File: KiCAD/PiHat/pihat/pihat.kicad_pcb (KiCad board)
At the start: 2 copper layers, 65 x 56 mm, 13 parts, among them P1 Conn_02x20_Odd_Even, Q1 BSS138, Q2 BSS138, U1 SG-92R, U2 SF3218MG

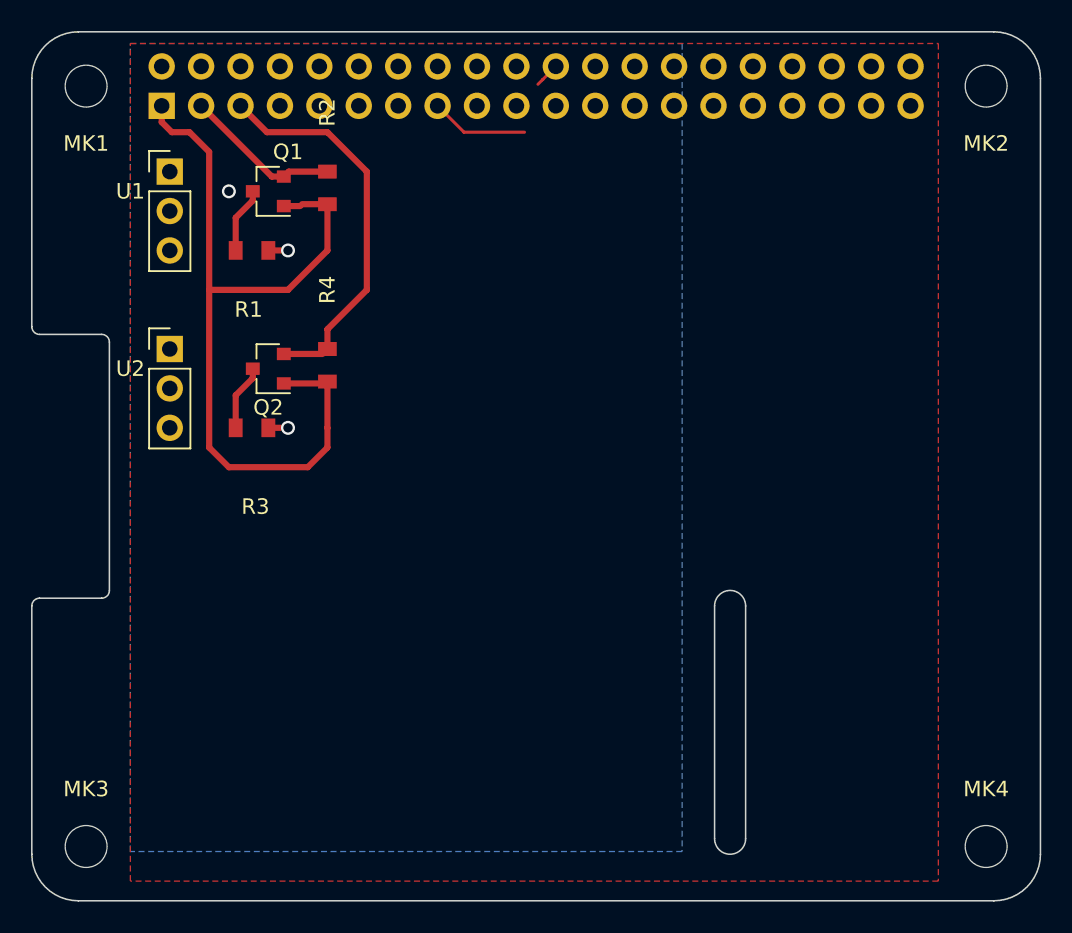
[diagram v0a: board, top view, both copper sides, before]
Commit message: compacted servo design
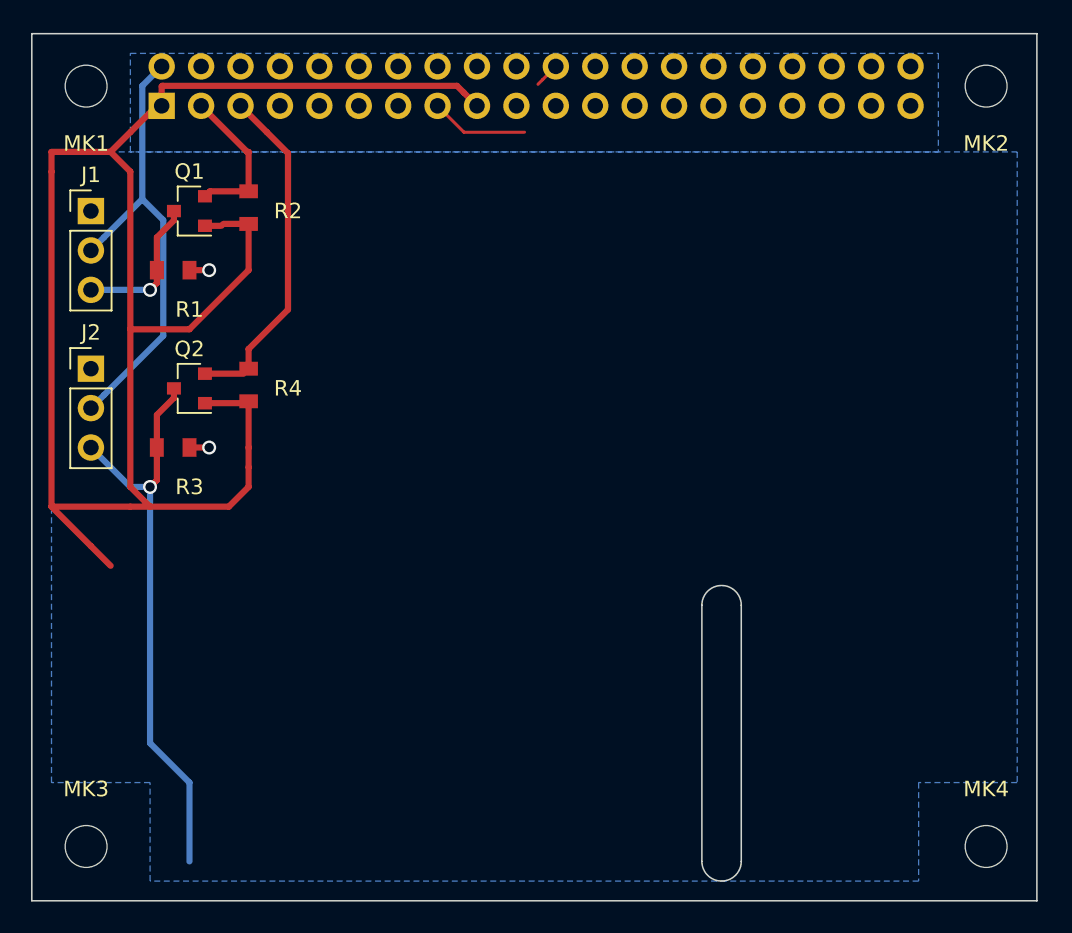
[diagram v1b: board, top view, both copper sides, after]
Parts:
- removed U1: SG-92R, trailTracer:PinHeader_1x03_P2.54mm_Vertical
- removed U2: SF3218MG, trailTracer:PinHeader_1x03_P2.54mm_Vertical
- added J1: Conn_01x03, Connector_PinHeader_2.54mm:PinHeader_1x03_P2.54mm_Vertical, F.Cu at (203.8, 105.5)
- added J2: Conn_01x03, Connector_PinHeader_2.54mm:PinHeader_1x03_P2.54mm_Vertical, F.Cu at (203.8, 115.7)
- moved Q2 5.24 mm to (210.2, 117.0)
- moved Q1 5.24 mm to (210.2, 105.5)
- moved R2 5.24 mm to (214.0, 104.3)
- moved R4 5.24 mm to (214.0, 115.7)
- moved R3 5.24 mm to (208.1, 120.8)
- moved R1 5.24 mm to (208.1, 109.4)
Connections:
- net /GPIO11(SPI0_SCK) renamed GPIO_11
- net /GPIO13(PWM1) renamed GPIO_13
- net /GPIO17(GEN0) renamed GPIO_17
- net /GPIO27(GEN2) renamed GPIO_27
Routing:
- net +3V3: track 54.2 -> 118.3 mm
- net Net-(J2-Pad3): track 4.27 -> 37.0 mm, vias 0 -> 1
- net +5V: track 2.54 -> 32.2 mm
- net Net-(J1-Pad3): track 4.27 -> 9.53 mm, vias 0 -> 1
- net GPIO_3: track 25.3 -> 22.2 mm
- net (no net): vias 1 -> 0
- added copper zone on B.Cu, net GND
- removed copper zone on B.Cu, net +5V
- removed copper zone on F.Cu, net GND
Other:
- board size 65 x 56 mm -> 64.8 x 55.9 mm
- board text removed: "DISPLAY"
- board text removed: "RJ45"
- board text removed: "USB"

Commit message: Added Fan Header
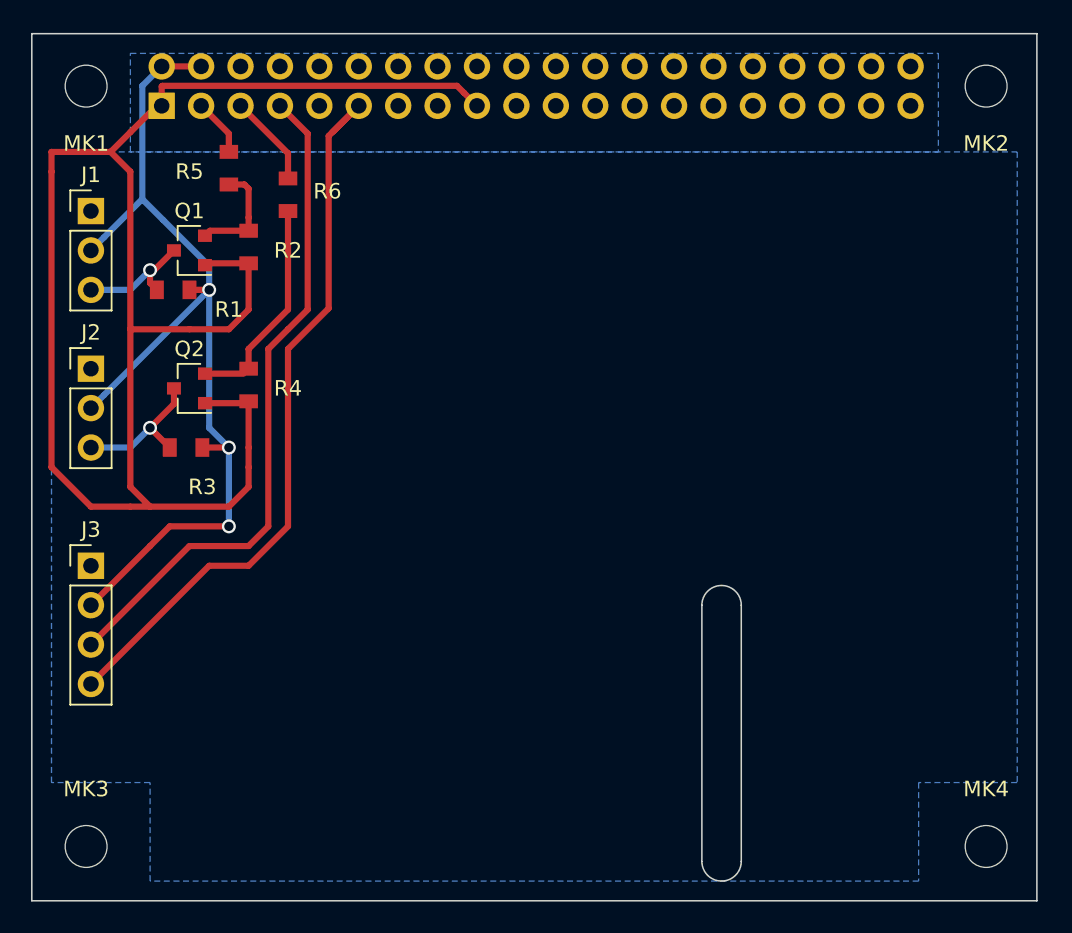
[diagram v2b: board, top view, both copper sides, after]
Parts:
- added J3: Fan, Connector_PinHeader_2.54mm:PinHeader_1x04_P2.54mm_Vertical, F.Cu at (203.8, 128.4)
- added R5: 220R, trailTracer:Yageo_R0805, F.Cu at (212.7, 103.8)
- added R6: 220R, trailTracer:Yageo_R0805, F.Cu at (216.5, 105.5)
- J1: value Conn_01x03 -> Pan Servo Connector
- J2: value Conn_01x03 -> Tilt Servo Connector
- moved Q1 2.54 mm to (210.2, 108.1)
- moved R2 2.54 mm to (214.0, 106.8)
- moved R1 1.27 mm to (208.1, 110.6)
- moved R3 0.83 mm to (208.9, 120.8)
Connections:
- P1 pad 7: /GPIO4(GCLK) -> GPIO_4
- Q1 pad 2: GPIO_2 -> Net-(Q1-Pad2)
- Q2 pad 2: GPIO_3 -> Net-(Q2-Pad2)
- R2 pad 1: GPIO_2 -> Net-(Q1-Pad2)
- R4 pad 1: GPIO_3 -> Net-(Q2-Pad2)
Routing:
- net GPIO_17: track 0.00 -> 48.3 mm
- net GPIO_4: track 0.00 -> 43.5 mm
- net +5V: track 32.2 -> 64.4 mm, vias 2 -> 3
- net Net-(J2-Pad3): track 37.0 -> 9.31 mm
- net GPIO_3: track 22.2 -> 5.95 mm
- net Net-(Q2-Pad2): track 0.00 -> 14.2 mm
- net +3V3: track 118.3 -> 110.4 mm
- net Net-(Q1-Pad2): track 0.00 -> 7.03 mm
- net GPIO_22: track 6.30 -> 0.00 mm
- net GPIO_2: track 9.77 -> 3.71 mm
- net Net-(J1-Pad3): track 9.53 -> 7.85 mm
- net GPIO_25: track 1.63 -> 0.00 mm

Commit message: Temporary Commit
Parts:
- added J4: Power Connector, Connector_JST:JST_VH_S2P-VH_1x02_P3.96mm_Horizontal, F.Cu at (249.5, 136.0)
- added U1: TPS5431DDA, Package_SO:TI_SO-PowerPAD-8_ThermalVias, F.Cu at (252.1, 119.5)
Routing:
- net +5V: track 64.4 -> 108.5 mm

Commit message: Minor commit
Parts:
- moved J3 6.35 mm to (203.8, 134.8), turned to 180 degrees
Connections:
- J3 pad 1: GND -> GPIO_17
- J3 pad 2: +5V -> GPIO_4
- J3 pad 3: GPIO_4 -> +5V
- J3 pad 4: GPIO_17 -> GND
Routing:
- net GPIO_17: track 48.3 -> 47.8 mm
- net +5V: track 108.5 -> 107.9 mm
- net GPIO_4: track 43.5 -> 43.0 mm

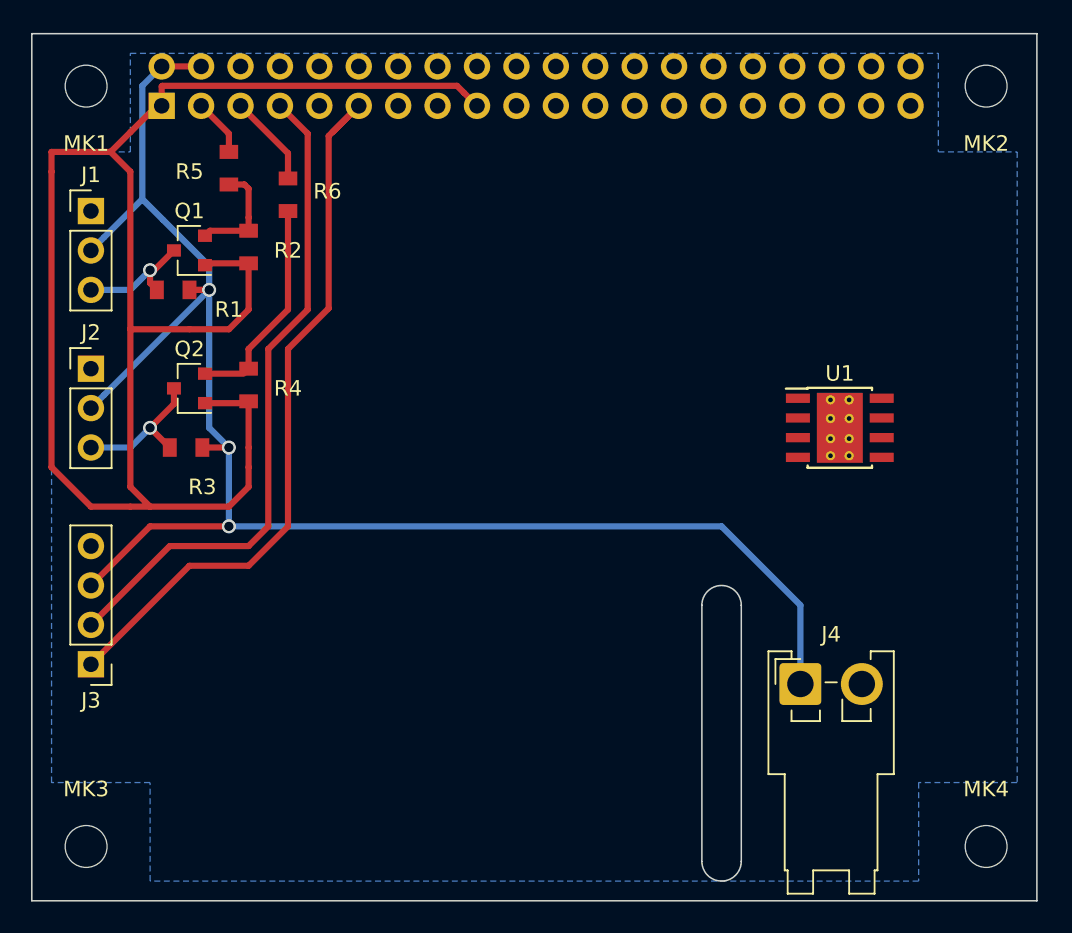
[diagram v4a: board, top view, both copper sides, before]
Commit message: Added status LEDs, power relay, organized traces
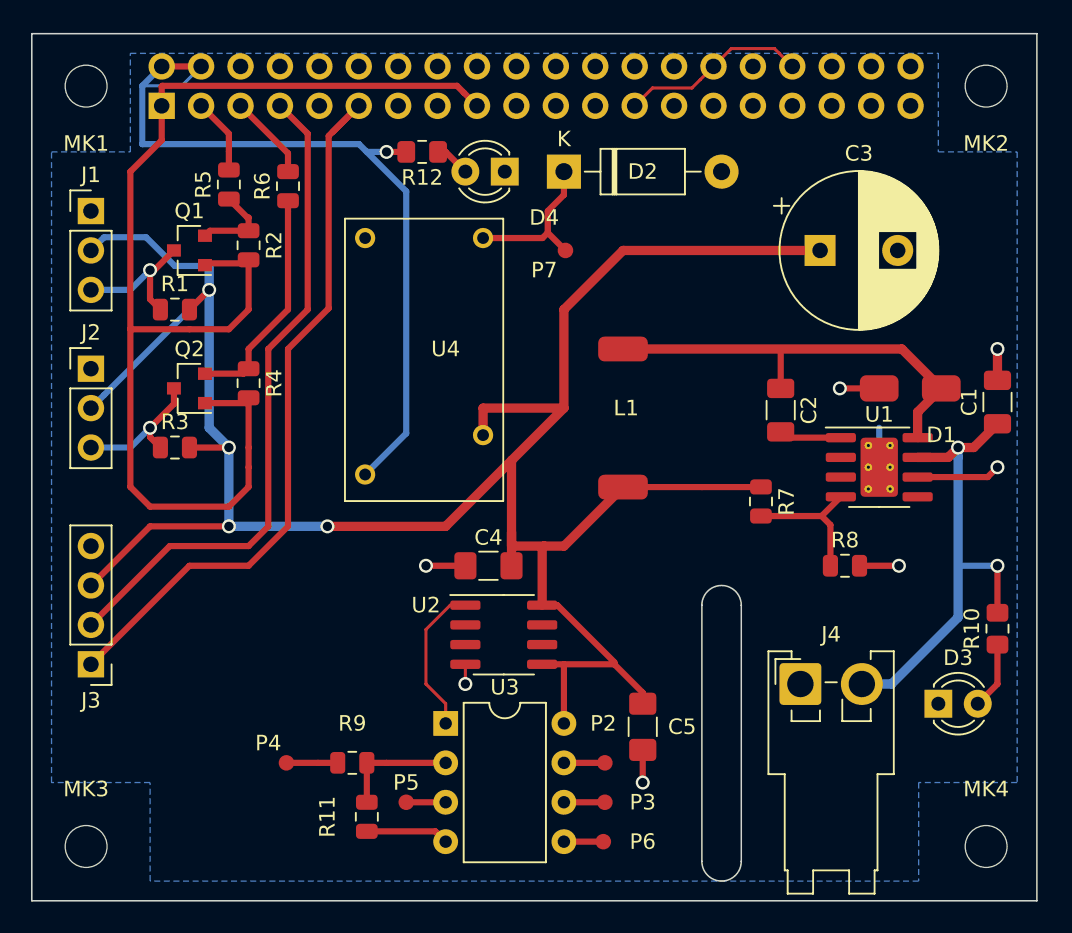
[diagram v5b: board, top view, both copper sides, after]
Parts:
- added C1: 100 uF, Resistor_SMD:R_1206_3216Metric, F.Cu at (262.2, 117.9)
- added C2: 10 nF, Resistor_SMD:R_1206_3216Metric, F.Cu at (248.3, 118.4)
- added C3: 270 uF, Capacitor_THT:CP_Radial_D10.0mm_P5.00mm, F.Cu at (250.8, 108.1)
- added C4: 10nF, Resistor_SMD:R_1206_3216Metric_Pad1.42x1.75mm_HandSolder, F.Cu at (229.4, 128.4)
- added C5: 220 uF, Capacitor_SMD:C_1206_3216Metric_Pad1.42x1.75mm_HandSolder, F.Cu at (239.4, 138.8)
- added D1: B340, trailTracer:DO-214, F.Cu at (258.6, 117.0)
- added D2: 1N4001, Diode_THT:D_DO-41_SOD81_P10.16mm_Horizontal, F.Cu at (234.3, 103.0)
- added D3: LED, LED_THT:LED_D3.0mm, F.Cu at (258.4, 137.3)
- added D4: LED, LED_THT:LED_D3.0mm, F.Cu at (230.5, 103.0)
- added L1: 15 uH, trailTracer:Coil, F.Cu at (238.1, 114.4)
- added P2: Pad, trailTracer:Pad, F.Cu at (236.8, 141.1)
- added P3: Pad, trailTracer:Pad, F.Cu at (236.8, 143.7)
- added P4: Pad, trailTracer:Pad, F.Cu at (216.5, 141.1)
- added P5: Pad, trailTracer:Pad, F.Cu at (224.1, 143.8)
- added P6: Pad, trailTracer:Pad, F.Cu at (236.8, 146.3)
- added P7: Pad, trailTracer:Pad, F.Cu at (234.3, 108.1)
- added R10: R_Small, Resistor_SMD:R_0805_2012Metric_Pad1.15x1.40mm_HandSolder, F.Cu at (262.2, 132.5)
- added R11: 10K, Resistor_SMD:R_0805_2012Metric, F.Cu at (221.6, 144.6)
- added R12: R_Small, Resistor_SMD:R_0805_2012Metric_Pad1.15x1.40mm_HandSolder, F.Cu at (225.2, 101.7)
- added R7: 10 KOhm, Resistor_SMD:R_0805_2012Metric, F.Cu at (247.0, 124.3)
- added R8: 3.24 KOhm, Resistor_SMD:R_0805_2012Metric, F.Cu at (252.4, 128.4)
- added R9: 15K, Resistor_SMD:R_0805_2012Metric, F.Cu at (220.7, 141.1)
- added U2: TMP36xS, Package_SO:SOIC-8_3.9x4.9mm_P1.27mm, F.Cu at (230.4, 132.9)
- added U3: ATTiny85, Package_DIP:DIP-8_W7.62mm, F.Cu at (226.7, 138.6)
- added U4: TE_OJ-SH-105LM, trailTracer:TE_OJ-SH-105LM, F.Cu at (230.5, 114.4)
- R1, R2, R3, R4, R5, R6: footprint trailTracer:Yageo_R0805 -> Resistor_SMD:R_0805_2012Metric
- U1: value TPS5431DDA -> TPS5430-Q1; footprint Package_SO:TI_SO-PowerPAD-8_ThermalVias -> Package_SO:SOIC-8-1EP_3.9x4.9mm_P1.27mm_EP2.41x3.81mm_ThermalVias
- moved U1 3.59 mm to (254.6, 122.1)
- moved R1 1.72 mm to (209.2, 111.9)
- moved R6 1.60 mm to (216.5, 103.9)
- moved R2 0.94 mm to (214.0, 107.8)
- moved R4 0.94 mm to (214.0, 116.6)
- moved R3 0.33 mm to (209.2, 120.8)
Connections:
- J4 pad 1: +5V -> GND
- J4 pad 2: GND -> Pi_Power+
- P1 pad 2: +5V -> PI_5V
- P1 pad 4: +5V -> PI_5V
- U1 pad 6: Net-(U1-Pad6) -> GND
- U1 pad 7: Net-(U1-Pad7) -> Pi_Power+
- U1 pad 9: Net-(U1-Pad9) -> GND
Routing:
- net PI_5V: track 0.00 -> 52.5 mm, vias 0 -> 1
- net +5V: track 107.9 -> 155.0 mm, vias 3 -> 4
- net GND: track 0.00 -> 38.5 mm, vias 0 -> 7
- net +3V3: track 110.4 -> 78.6 mm
- net Pi_Power+: track 0.00 -> 30.5 mm, vias 0 -> 2
- net Net-(C2-Pad1): track 0.00 -> 27.9 mm
- net Net-(D2-Pad1): track 0.00 -> 10.3 mm
- net Net-(U2-Pad1): track 0.00 -> 9.77 mm
- net Net-(R7-Pad2): track 0.00 -> 9.10 mm
- net Net-(R11-Pad1): track 0.00 -> 7.62 mm
- net Net-(D3-Pad2): track 0.00 -> 4.34 mm
- net Net-(C2-Pad2): track 0.00 -> 4.03 mm
- net Net-(P4-Pad1): track 0.00 -> 3.31 mm
- net Net-(P3-Pad1): track 0.00 -> 2.64 mm
- net Net-(P2-Pad1): track 0.00 -> 2.64 mm
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
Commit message: Peer review changes
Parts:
- R10: value R_Small -> 470
- R12: value R_Small -> 120R
- moved C5 5.43 mm to (237.5, 133.7)
- moved D4 0.64 mm to (231.1, 103.0)
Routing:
- net GND: track 38.5 -> 58.6 mm
- net +5V: track 155.0 -> 151.4 mm
- net Net-(D4-Pad2): track 2.29 -> 2.92 mm

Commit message: Revision 1
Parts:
- added C6: 47 uF, Capacitor_SMD:C_1206_3216Metric_Pad1.42x1.75mm_HandSolder, F.Cu at (262.2, 124.8)
- added F1: 5A Medium Blow, Resistor_SMD:R_0603_1608Metric_Pad1.05x0.95mm_HandSolder, F.Cu at (254.2, 131.6)
- C1: value 100 uF -> 47 uF; footprint Resistor_SMD:R_1206_3216Metric -> Capacitor_SMD:C_1206_3216Metric_Pad1.42x1.75mm_HandSolder
- L1: footprint trailTracer:Coil -> trailTracer:SRR1050A Coil
- moved D2 32.1 mm to (221.0, 132.2), turned to 180 degrees
- moved P7 23.8 mm to (221.0, 127.8)
- moved C3 15.3 mm to (236.2, 112.5)
- moved U4 11.1 mm to (219.7, 117.0), turned to 90 degrees
- moved C4 10.6 mm to (237.9, 134.8), turned to 180 degrees
- moved R11 5.85 mm to (222.9, 138.9)
- moved L1 5.68 mm to (240.6, 119.5)
- moved R7 4.44 mm to (248.6, 128.4), turned to 0 degrees
- moved P4 3.86 mm to (220.3, 141.7)
- moved P6 3.81 mm to (240.6, 146.2)
- moved R9 2.26 mm to (220.3, 138.9), turned to 270 degrees
- moved C5 2.16 mm to (237.9, 131.6), turned to 0 degrees
- moved P3 1.91 mm to (238.7, 143.7)
- moved P5 1.80 mm to (222.9, 145.0)
- moved R8 0.63 mm to (253.0, 128.4)
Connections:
- C1 pad 1: Pi_Power+ -> +12V
- J4 pad 2: Pi_Power+ -> Net-(F1-Pad1)
- R10 pad 2: Pi_Power+ -> +12V
- U1 pad 7: Pi_Power+ -> +12V
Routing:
- net Pi_Power+: track 30.5 -> 0.00 mm, vias 2 -> 0
- net +5V: track 151.4 -> 120.9 mm, vias 4 -> 3
- net +12V: track 0.00 -> 26.8 mm, vias 0 -> 2
- net PI_5V: track 52.5 -> 41.0 mm
- net Net-(F1-Pad1): track 0.00 -> 4.51 mm
- net Net-(P6-Pad1): track 2.54 -> 6.39 mm
- net Net-(C2-Pad1): track 27.9 -> 24.8 mm
- net Net-(D2-Pad1): track 10.3 -> 8.19 mm
- net Net-(R7-Pad2): track 9.10 -> 7.03 mm
- net Net-(P3-Pad1): track 2.64 -> 4.55 mm
- net Net-(P5-Pad1): track 2.54 -> 4.34 mm
- net Net-(P4-Pad1): track 3.31 -> 1.98 mm
- net Net-(R11-Pad1): track 7.62 -> 8.70 mm
- net GND: track 58.6 -> 59.4 mm, vias 7 -> 8
